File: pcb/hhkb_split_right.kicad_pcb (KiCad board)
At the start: 4 copper layers, 173.7 x 97.4 mm, 84 parts, among them SW1 6, SW10 Y, SW11 U, SW12 I, SW13 O, SW14 P, SW15 [, SW16 ], SW17 Del, SW18 H, SW19 J, SW2 7, SW20 K, SW21 L, SW22 ;, SW23 ', SW24 Enter, SW25 N, SW26 M, SW27 ,, SW28 ., SW29 /, SW3 8, SW30 Shift, SW31 Fn, SW32 R-Space, SW33 Meta, SW34 Alt, SW4 9, SW5 0, SW6 -, SW7 =, SW8 \, SW9 `, U1 74LVC595, U2 74LVC595

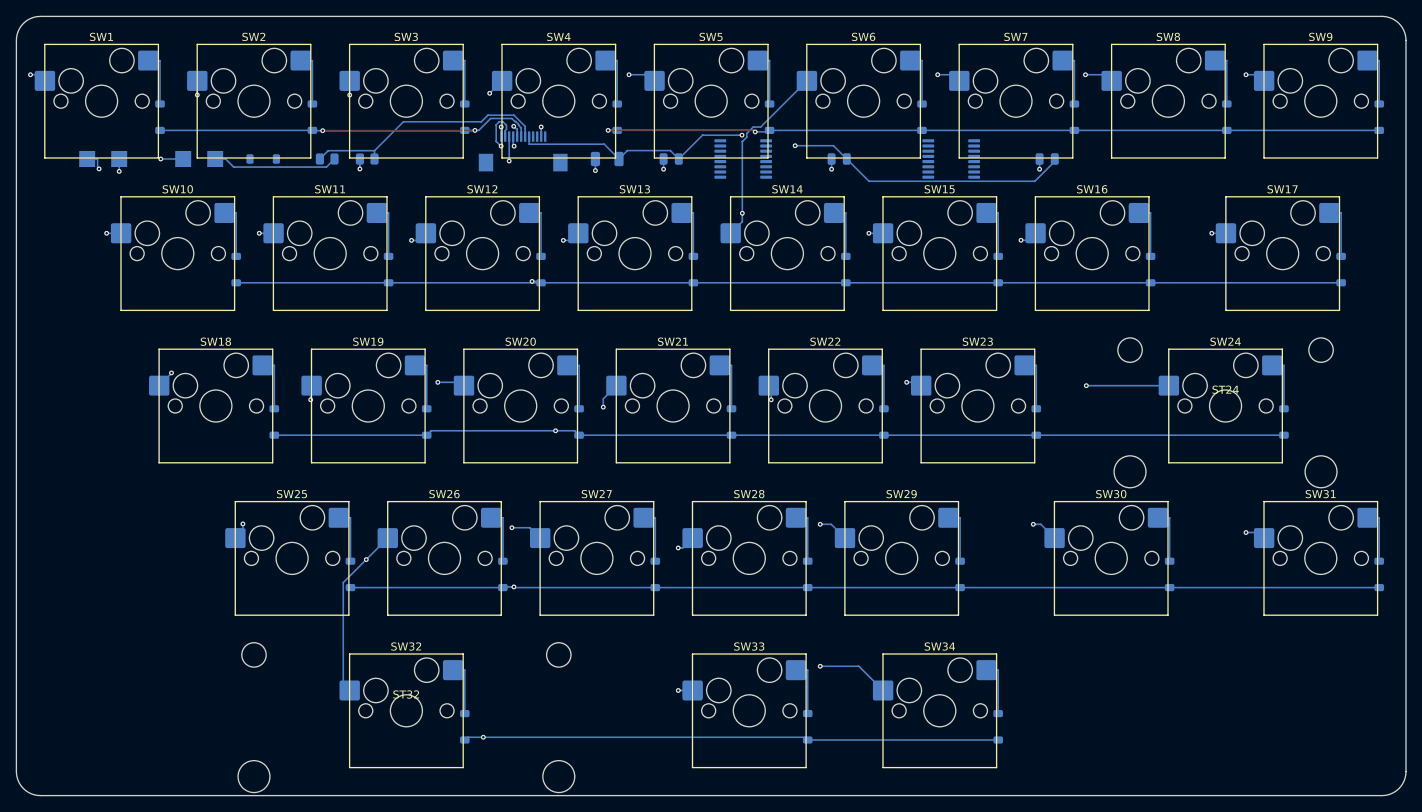
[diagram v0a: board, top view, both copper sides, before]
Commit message: マトリクスのダイオードを BAT46W にした（1N4148W はバックアップとして記録）
在庫 5,000 超の SOD-123 ショットキー 29 件、BAT47/48/49/54/85、1SS 系、
NSR、RB751、PMEG、MBR05xx、SS12、1N5711、BAS40 を当たった。
**VF と IR を両方「動作点で」保証しているのは BAT46W だけ。**

  BAT46W(C54110)  VF≦0.25V@0.1mA   IR≦0.3µA@1.5V   $6.76(122個+段取り)
  1N4148W(C81598) なし(1mA 0.715V) なし(20V 25nA)  $1.43 Basic
  SD103AW         0.37V@20mA       なし(30V 5µA)   $6.75
  BAT54W          240mV@0.1mA      なし(25V 2µA)   $6.25

罠: BAT48ZFILM-FS(C7436546) は名前だけで中身は SD103AW と同じ仕様。

## 効果

打ち止めがマイコン律速に戻る（1.20 → **1.10V/本**）。
**壊れ方が「一部のキーが反応しない」から「電源が落ちる」に変わる。**
実測が不要になる。

## 代償（数字で押さえた）

+約 ¥800。逆漏れ 12 倍で **60℃ かつ 5 個以上の同時押しだと余裕を割る**
（25℃ なら 9 個でも OK）。接合容量 5 倍だが列切替後 2.31µs に対し
SPI 転送で 4.0µs 以上空くので間に合う。

## 検査を 2 つ足した

  test_the_matrix_reads_high_at_the_cutoff … 打ち止めで行が VIH に届くか
  test_ghosting_survives_a_full_row_of_simultaneous_presses … 逆漏れの合計

どちらも故意に壊して検出を確認した。**1 回目は __pycache__ が古いまま
（同じ秒に書き換えたため）で検出できていなかった。**破壊試験のあとは
バイトコードを消すこと。

open-gaps #25 に「電池が尽きるときの止まり方」を記録した。マイコンの
ブラウンアウトは起動と広告を繰り返しうるし、**低電圧の flash 書き込みで
ペアリング情報が壊れうる**。POFCON か soft-off で自分から止めれば直るが、
ZMK に機能が無いので自作が要る。**基板に影響しないので届いてからでよい。**

3 基板とも DRC 0 / 未配線 0。検査 294 件。

Co-Authored-By: Claude Opus 5 (1M context) <noreply@anthropic.com>
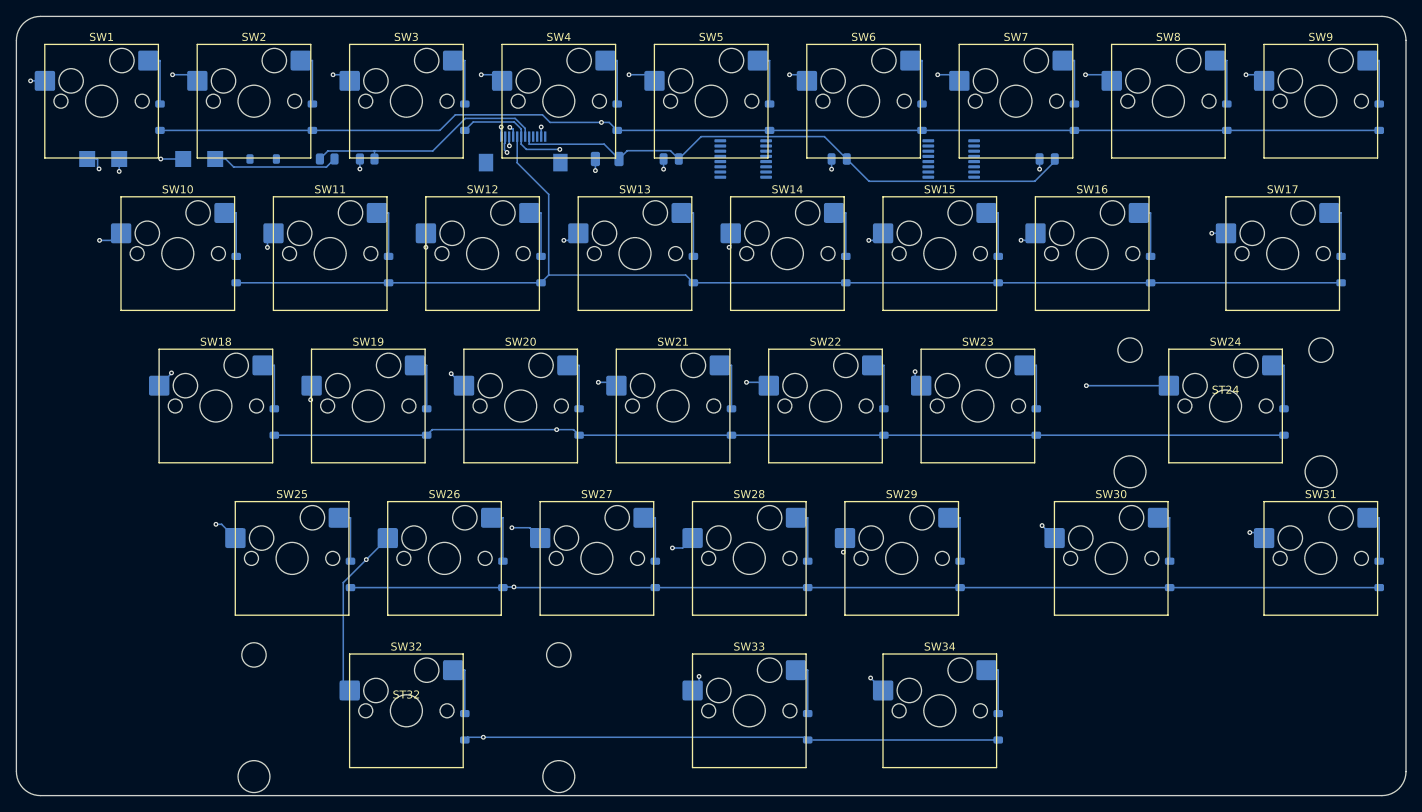
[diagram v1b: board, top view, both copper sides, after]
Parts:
- D1, D10, D11, D12, D13, D14, D15, D16, D17, D18, D19, D2, D20, D21, D22, D23, D24, D25, D26, D27, D28, D29, D3, D30, D31, D32, D33, D34, D4, D5, D6, D7, D8, D9: value 1N4148W -> BAT46W
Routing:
- net ROW0: track 164.0 -> 175.5 mm, vias 4 -> 2
- net ROW4: track 154.4 -> 147.8 mm
- net ROW1: track 164.1 -> 157.9 mm, vias 2 -> 0
- net COL1: track 74.2 -> 80.1 mm
- net COL2: track 90.1 -> 94.1 mm
- net ROW2: track 166.5 -> 169.3 mm
- net COL8: track 67.7 -> 70.3 mm
- net COL5: track 99.8 -> 97.2 mm, vias 4 -> 5
- net COL7: track 85.5 -> 84.2 mm
- net COL0: track 27.7 -> 28.4 mm
- net COL4: track 99.5 -> 99.0 mm
- net VBATT_SENSE: track 30.8 -> 30.3 mm
- net COL3: track 75.4 -> 74.9 mm
- net V3V3: track 73.2 -> 73.1 mm, vias 2 -> 0

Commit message: #23 の D9 移設を実施した（アンテナ実外形の真下の配線が 0 本になった）
- ROW4 の行き先を D5（左列）→ D9（右列・元 MISO）へ。TX 側レーン 6 → 5 本、
  LANE_STEP 0.7 → 0.65。最内レーン -3.8mm はアンテナ実外形（-3.65〜-0.15）の外
- ケーブルのピン配置は ROW4 を右群 4 番へ（左群のままだと横枝が縦線を
  8 箇所で横切る。DRC で実測）。本体基板 2 枚も再生成＋再配線。3 基板 DRC 0
- ファームは row-gpios を D9 へ、&spi2_default/&spi2_sleep の psels から
  MISO を外して P1.14 を解放（CI ビルド・実機は未確認）
- 買い物リストを shopping-list.md に統合（#22 の再発防止の作法つき）
- Task C3 §6-6b に測定条件欄を追加
- 全検査 386 passed / 3 skipped

Co-Authored-By: Claude Fable 5 <noreply@anthropic.com>
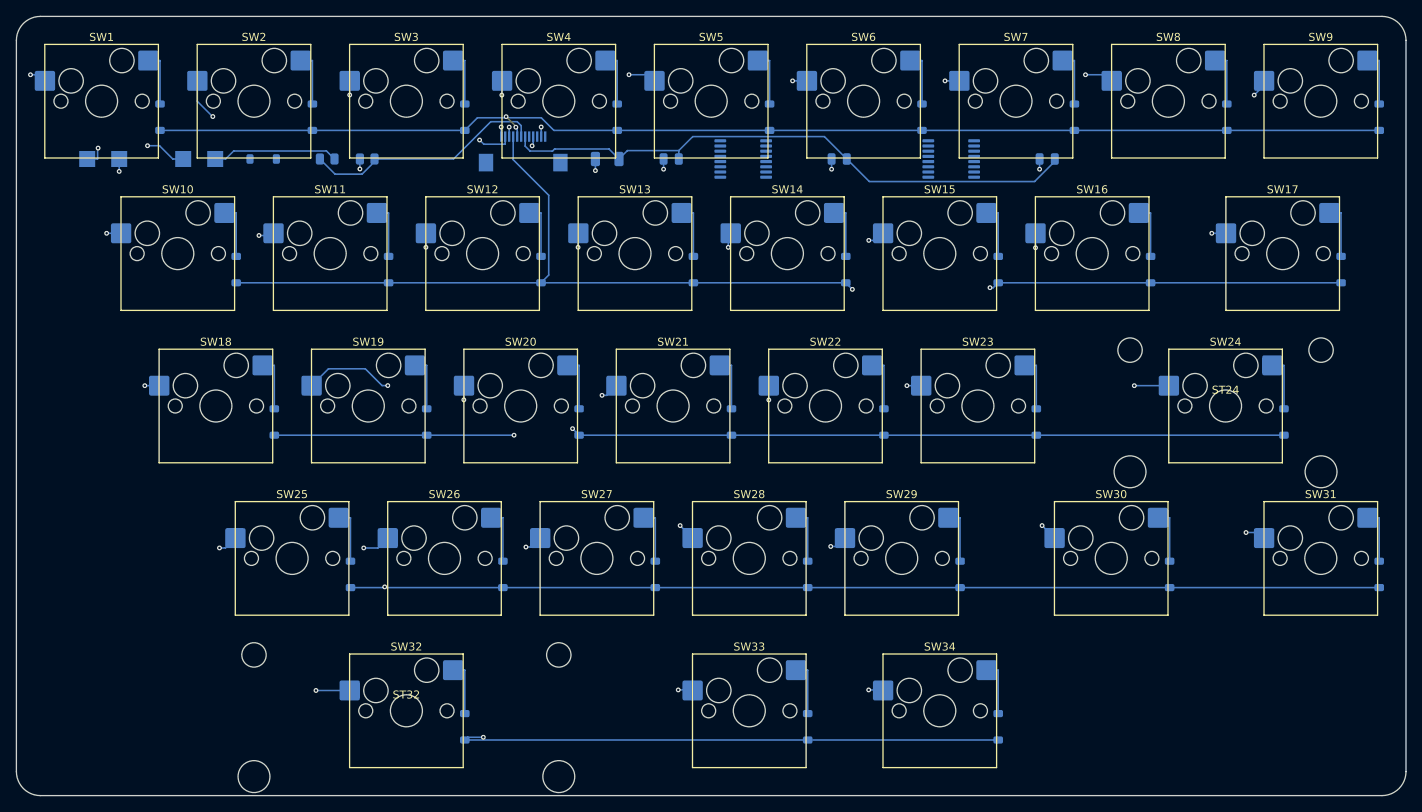
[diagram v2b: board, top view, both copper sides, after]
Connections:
- J_DB pad 10: ROW3 -> ROW2
- J_DB pad 11: ROW4 -> ROW3
- J_DB pad 4: SPI_MOSI -> ROW4
- J_DB pad 5: V3V3 -> SPI_MOSI
- J_DB pad 6: VBATT_SENSE -> V3V3
- J_DB pad 7: ROW0 -> VBATT_SENSE
- J_DB pad 8: ROW1 -> ROW0
- J_DB pad 9: ROW2 -> ROW1
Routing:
- net ROW0: track 175.5 -> 156.9 mm
- net COL2: track 94.1 -> 103.1 mm, vias 3 -> 4
- net ROW4: track 147.8 -> 153.3 mm
- net COL8: track 70.3 -> 65.3 mm
- net ROW3: track 189.5 -> 193.8 mm
- net COL7: track 84.2 -> 80.9 mm
- net COL4: track 99.0 -> 96.5 mm
- net COL1: track 80.1 -> 77.6 mm
- net COL3: track 74.9 -> 73.2 mm
- net COL6: track 50.3 -> 52.0 mm
- net ROW1: track 157.9 -> 159.3 mm, vias 0 -> 2
- net ROW2: track 169.3 -> 170.6 mm, vias 2 -> 3
- net V3V3: track 73.1 -> 74.2 mm
- net COL5: track 97.2 -> 96.2 mm
- net COL0: track 28.4 -> 27.7 mm

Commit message: ★ 電池蓋を差し込み式にし、本体基板に固定を入れた（#35 / #36）
電池蓋（#35）: コブの奥面へ移し、留め方を 3 度作り直した。片持ちばね案は
**原理的に外れない**（腕が壁の裏に立っていて、どう撓ませても抜けない。
逃がす先の内側は電池が埋めている）。断面を描いて分かった。採用したのは
下へスライドして庇の裏へ舌を差し込む形で、重力が留める側に効く。
検査は「留まる」と「外せる」を必ず一緒に見る——前者だけでは不成立案が通った。

本体基板（#36）: 取付穴 6/8 とプレート裏の柱・M2 ネジ。穴の探索が
コートヤードしか見ておらず、柱がキーとプレート開口に当たっていた。
柱の検査は assert がループの中にあって 1 本目で止まっており、3 往復した。

その他: 自動配線器がたまに 0.12mm の線を引いて DRC が赤になるので、
取り込み後に幅を揃えるようにした（配線するたびに赤が出たり出なかったり
していた）。CAD を変えたら絵を出し直す手順を tools/refresh_view.sh に。

検査 395 件 緑 / DRC 3 基板とも 0 違反・0 未配線

Co-Authored-By: Claude Opus 5 (1M context) <noreply@anthropic.com>
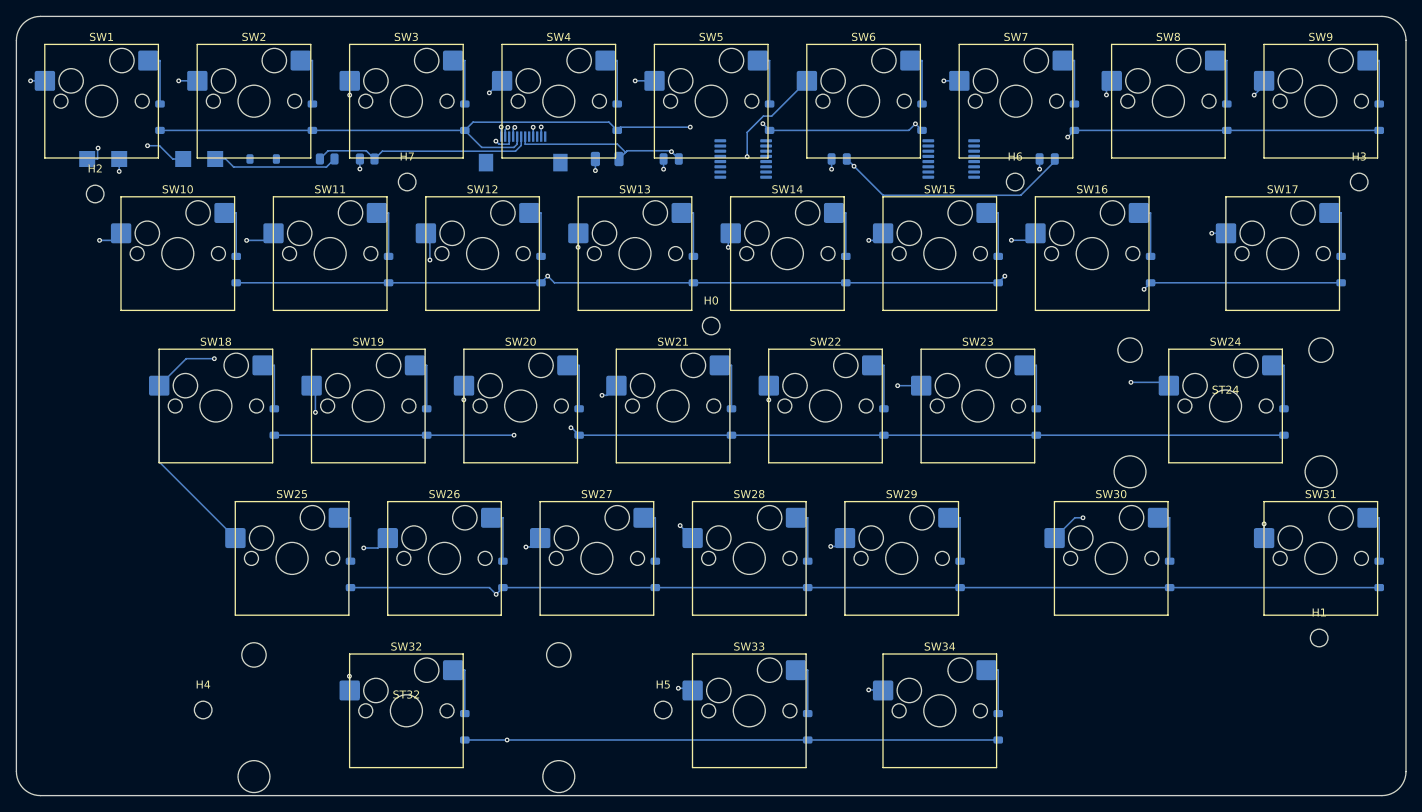
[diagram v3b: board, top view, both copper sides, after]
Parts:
- added H0: MountingHole_2.2mm_M2, MountingHole_2.2mm_M2, F.Cu at (150.0, 90.0)
- added H1: MountingHole_2.2mm_M2, MountingHole_2.2mm_M2, F.Cu at (226.0, 129.0)
- added H2: MountingHole_2.2mm_M2, MountingHole_2.2mm_M2, F.Cu at (73.0, 73.5)
- added H3: MountingHole_2.2mm_M2, MountingHole_2.2mm_M2, F.Cu at (231.0, 72.0)
- added H4: MountingHole_2.2mm_M2, MountingHole_2.2mm_M2, F.Cu at (86.5, 138.0)
- added H5: MountingHole_2.2mm_M2, MountingHole_2.2mm_M2, F.Cu at (144.0, 138.0)
- added H6: MountingHole_2.2mm_M2, MountingHole_2.2mm_M2, F.Cu at (188.0, 72.0)
- added H7: MountingHole_2.2mm_M2, MountingHole_2.2mm_M2, F.Cu at (112.0, 72.0)
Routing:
- net COL2: track 103.1 -> 90.1 mm
- net ROW0: track 156.9 -> 165.0 mm, vias 2 -> 4
- net ROW2: track 170.6 -> 175.1 mm
- net ROW3: track 193.8 -> 197.2 mm
- net ROW4: track 153.3 -> 150.2 mm
- net COL7: track 80.9 -> 83.6 mm
- net VBATT_SENSE: track 30.4 -> 27.8 mm
- net ROW1: track 159.3 -> 161.7 mm, vias 2 -> 4
- net COL4: track 96.5 -> 94.9 mm
- net V3V3: track 74.2 -> 75.7 mm, vias 0 -> 2
- net COL6: track 52.0 -> 50.5 mm
- net COL3: track 73.2 -> 74.6 mm
- net COL0: track 27.7 -> 28.4 mm
- net COL8: track 65.3 -> 65.8 mm
- net COL1: track 77.6 -> 77.3 mm, vias 4 -> 3

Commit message: 2 層化と GND ベタ両面化、GND ビアの大量投入（指摘 2/3/4/5/8）
**まだ未配線が残っている途中状態**（左 1・右 3）。DRC 違反は 3 基板とも 0。

指摘 2（2 層化）
  4 層にした当時の根拠「行の引き回しが 2 層では通らない」は、その後
  Freerouting に切り替えたときに崩れていた。実測すると信号は In2.Cu と
  B.Cu の 2 層に収まり、**F.Cu は配線 0 本で丸ごと空いていた。**
  決定記録がその事実に追いついていなかった。

指摘 3（GND ベタ）
  F.Cu と B.Cu の両面に敷いた。4 層のときのように GND 専用層を
  自動配線器から予約することはできない（信号層と兼ねるため）。

指摘 4/5（GND ビア）
  ファンアウト（パッド→地板）に加えて 2 種類足した。

    格子状のスティッチング   左 175 / 右 210
    長い配線の脇のビアフェンス 左 121 / 右 174

  **ビアフェンスの目的は離島の救済ではない。**信号の戻り電流は配線の
  直近を流れたがるが、長い配線がベタを割ると、戻り電流はスリットの端まで
  大回りするしかない。配線をまたぐ位置にビアがあれば、反対面を経由して
  その場で横断できる。「繋がっている」と「最短で行ける」は別。

指摘 8（電源を太く）
  **ネットクラスを 2 つに割った**（KiCad は複数クラスを DSN に書き出し、
  Freerouting も受け取る。生の DSN を読んで確認した）。

    PowerFFC   V3V3       0.30mm  ← FFC のパッドが 0.30mm 幅で、これが上限
    PowerWide  GND ほか   0.60mm  ← 細ピッチのパッドに繋がらないので太くできる

  当初 0.5mm 一律にしたら V3V3 が J_DB に届かず未配線になった。
  測ったら Hirose FH12-12S-0.5SH のパッドは幅 0.30mm・隙間 0.20mm で、
  **0.5mm の線は物理的に載らない。**

自分のコードで踏んだ落とし穴（どれも実測で見つけた）
  - `pad is skip` で自分を除外 → SWIG は毎回別プロキシを返すので効かず、
    ファンアウトが 0 個になった
  - 箱どうしの重なりで当たり判定 → 丸いビアには厳しすぎ、0.65mm ピッチの
    TSSOP でビアが 1 つも置けなかった
  - **フットプリントの外接箱を障害物にした** → MX スイッチが約 19mm 角
    あるため基板全面が「置けない」ことになり、格子点の 8 割が飛んだ。
    実際に妨げるのはパッドと穴なので、そちらで見るようにした
  - ビア半径を二重に数えていた（0.3mm 過剰に保守的）→ 10.8mm² の離島でも
    格子点 48 個が全部「置けない」判定だった

配線後に 1 本ずつ太らせる後処理（gnd_fanout.widen）は**外した。**
自前の当たり判定が取りこぼして DRC 違反を 3 回続けて出したのと、
指摘 8 はクラス分けで達成できているため。実装は残してある。

Co-Authored-By: Claude Sonnet 5 <noreply@anthropic.com>
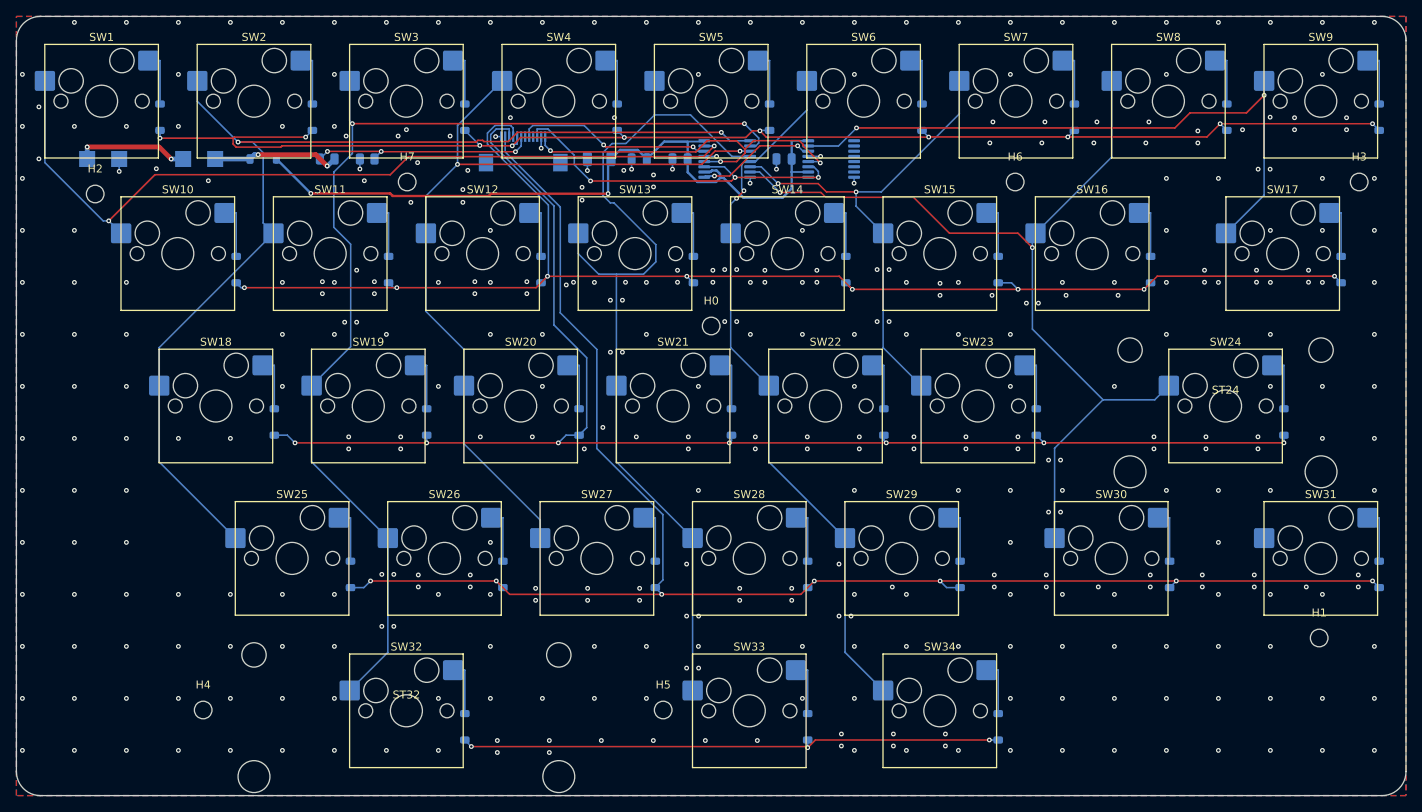
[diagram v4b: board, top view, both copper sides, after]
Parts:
- removed C_MCU: cap_100n, C_0805_2012Metric
- added C_RAIL: cap_100n, C_0805_2012Metric, B.Cu at (141.0, 69.1)
- moved C_U2 32.9 mm to (159.1, 69.1)
- moved C_U1 19.9 mm to (146.1, 69.1)
- moved U2 15.0 mm to (165.0, 69.1)
- moved U1 2.00 mm to (152.0, 69.1)
- moved C_BULK 1.00 mm to (136.0, 69.1)
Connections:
- D_PWR pad 1: (no net) -> V3V3
- D_PWR pad 2: (no net) -> VBATT_SW
- U1 pad 1: (no net) -> COL1
- U1 pad 10: (no net) -> V3V3
- U1 pad 11: (no net) -> SPI_SCK
- U1 pad 12: (no net) -> CS
- U1 pad 13: (no net) -> GND
- U1 pad 14: (no net) -> SPI_MOSI
- U1 pad 15: (no net) -> COL0
- U1 pad 16: (no net) -> V3V3
- U1 pad 2: (no net) -> COL2
- U1 pad 3: (no net) -> COL3
- U1 pad 4: (no net) -> COL4
- U1 pad 5: (no net) -> COL5
- U1 pad 6: (no net) -> COL6
- U1 pad 7: (no net) -> COL7
- U1 pad 8: (no net) -> GND
- U1 pad 9: (no net) -> U1_U2
- U2 pad 10: (no net) -> V3V3
- U2 pad 11: (no net) -> SPI_SCK
- U2 pad 12: (no net) -> CS
- U2 pad 13: (no net) -> GND
- U2 pad 14: (no net) -> U1_U2
- U2 pad 15: (no net) -> COL8
- U2 pad 16: (no net) -> V3V3
- U2 pad 8: (no net) -> GND
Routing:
- net ROW4: track 150.2 -> 68.4 mm, vias 2 -> 3
- net COL0: track 28.4 -> 104.2 mm
- net COL1: track 77.3 -> 137.1 mm, vias 3 -> 2
- net COL2: track 90.1 -> 139.5 mm, vias 4 -> 2
- net SPI_SCK: track 0.00 -> 46.3 mm, vias 0 -> 3
- net CS: track 0.00 -> 46.1 mm, vias 0 -> 3
- net COL7: track 83.6 -> 115.6 mm, vias 4 -> 2
- net COL3: track 74.6 -> 104.3 mm, vias 4 -> 2
- net SPI_MOSI: track 0.00 -> 24.4 mm, vias 0 -> 2
- net COL4: track 94.9 -> 113.3 mm, vias 5 -> 0
- net V3V3: track 75.7 -> 93.4 mm
- net U1_U2: track 0.00 -> 14.9 mm, vias 0 -> 2
- net COL8: track 65.8 -> 80.6 mm, vias 3 -> 2
- net ROW1: track 161.7 -> 175.3 mm, vias 4 -> 8
- net COL6: track 50.5 -> 63.2 mm, vias 3 -> 2
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- added copper zone on B.Cu, net GND
- added copper zone on F.Cu, net GND
- removed copper zone on In1.Cu, net GND
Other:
- copper layers 4 -> 2
